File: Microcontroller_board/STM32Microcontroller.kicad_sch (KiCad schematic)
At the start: 0 parts

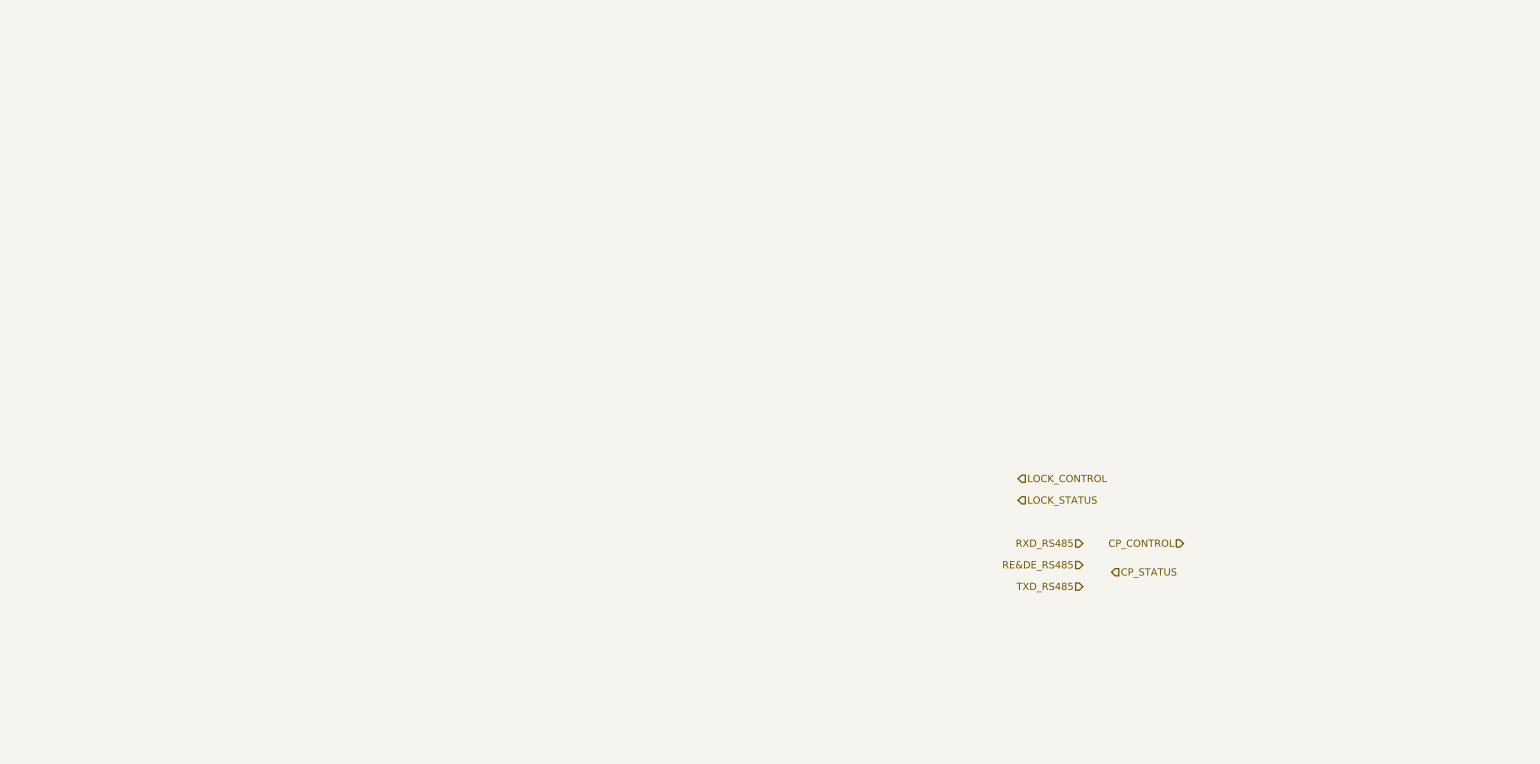
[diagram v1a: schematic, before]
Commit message: CP circuit added as in the PRIMO charger
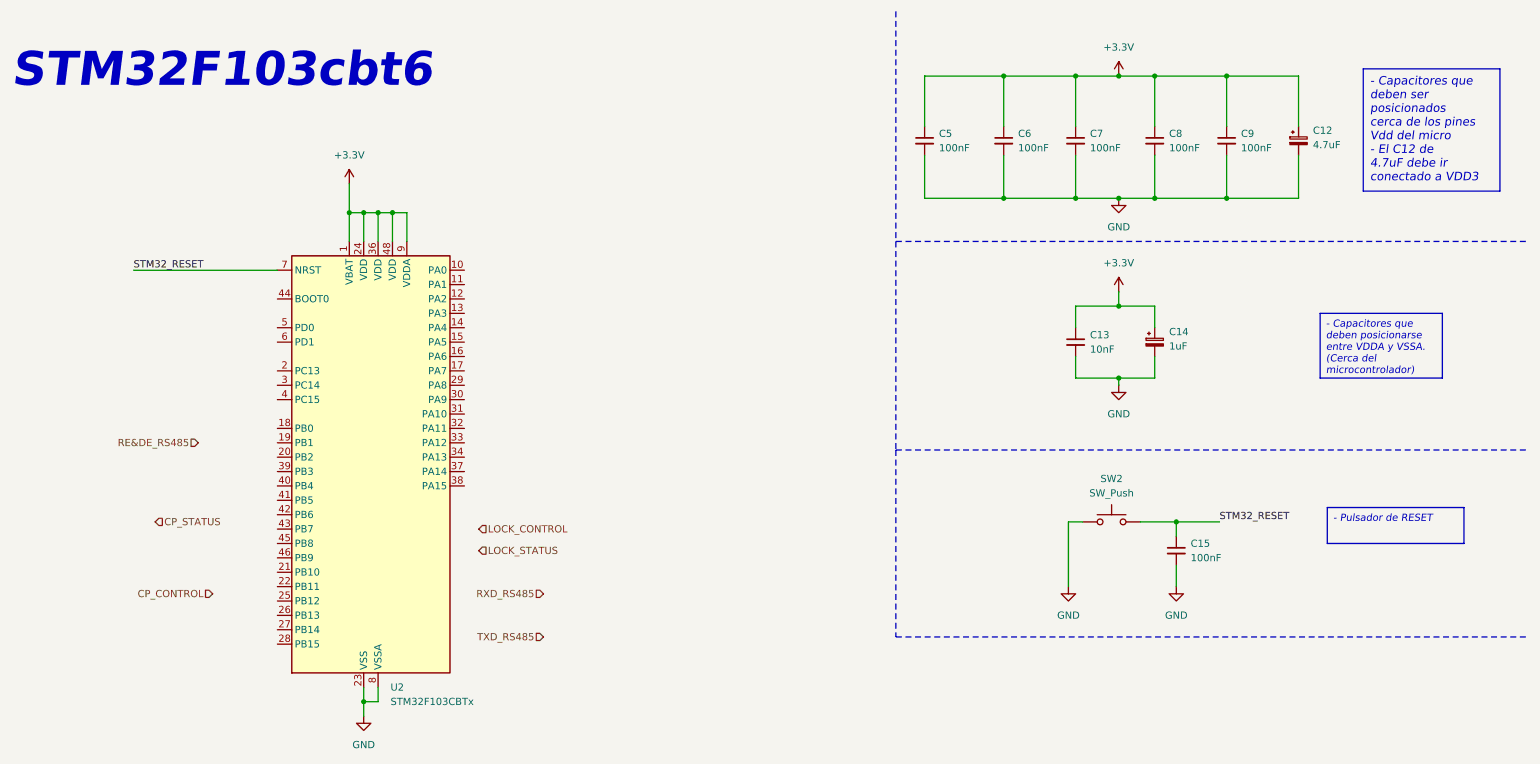
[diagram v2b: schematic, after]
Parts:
- added C12: 4.7uF, symbol Device:C_Polarized_Small
- added C13: 10nF, symbol Device:C_Small
- added C14: 1uF, symbol Device:C_Polarized_Small
- added C15, C5, C6, C7, C8, C9: 100nF, symbol Device:C_Small
- added SW2: SW_Push, symbol Switch:SW_Push
- added U2: STM32F103CBTx, Package_QFP:LQFP-48_7x7mm_P0.5mm, symbol MCU_ST_STM32F1:STM32F103CBTx
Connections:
- new net +3.3V: C12.1, C13.1, C14.1, C5.1, C6.1, C7.1, C8.1, C9.1, U2.1 (VBAT), U2.24 (VDD), U2.36 (VDD), U2.48 (VDD), U2.9 (VDDA)
- new net GND: C12.2, C13.2, C14.2, C15.2, C5.2, C6.2, C7.2, C8.2, C9.2, SW2.1, U2.23 (VSS), U2.35 (VSS), U2.47 (VSS), U2.8 (VSSA)
- new net STM32_RESET: C15.1, SW2.2, U2.7 (NRST)
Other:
- note added: "STM32F103cbt6"

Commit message: Added led interface
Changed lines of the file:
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@@
   )
   (text_box "- Pulsador de RESET"
-    (at 248.92 99.06 0) (size 24.13 6.35)
+    (at 256.54 99.06 0) (size 24.13 6.35)
     (stroke (width 0) (type default))
     (fill (type color) (color 255 227 142 1))
@@
   )
   (text_box "- Capacitores que deben ser posicionados cerca de los pines Vdd del micro\n- El C12 de 4.7uF debe ir conectado a VDD3\n\n"
-    (at 255.27 21.59 0) (size 24.13 21.59)
+    (at 255.27 21.59 0) (size 25.4 22.86)
     (stroke (width 0) (type default))
     (fill (type color) (color 255 227 142 1))
@@
   )
   (text_box "- Capacitores que deben posicionarse entre VDDA y VSSA.\n(Cerca del microcontrolador)"
-    (at 247.65 64.77 0) (size 21.59 11.43)
+    (at 256.54 64.77 0) (size 24.13 12.7)
     (stroke (width 0) (type default))
     (fill (type color) (color 255 227 142 1))
@@
     (effects (font (size 1.27 1.27)) (justify right))
   )
+  (hierarchical_label "LED_CONTROL" (shape input) (at 99.06 125.73 0) (fields_autoplaced)
+    (effects (font (size 1.27 1.27)) (justify left))
+  )
   (hierarchical_label "RE&DE_RS485" (shape input) (at 49.53 87.63 180) (fields_autoplaced)

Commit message: Added connector for st link programmer
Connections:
- net SWDIO: now reaches U2.34 (PA13)
- net SWCLK: now reaches U2.37 (PA14)
- net STM32_RESET renamed NRST
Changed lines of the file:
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@@
-    (stroke (width 0) (type default))
-  )
-  (wire (pts (xy 38.1 57.15) (xy 63.5 57.15))
     (stroke (width 0) (type default))
   )
@@
     (stroke (width 0) (type default))
   )
+  (wire (pts (xy 96.52 90.17) (xy 104.14 90.17))
+    (stroke (width 0) (type default))
+  )
+  (wire (pts (xy 96.52 92.71) (xy 104.14 92.71))
+    (stroke (width 0) (type default))
+  )
   (wire (pts (xy 231.14 22.86) (xy 218.44 22.86))
     (stroke (width 0) (type default))
@@
   )
   (wire (pts (xy 177.8 44.45) (xy 191.77 44.45))
+    (stroke (width 0) (type default))
+  )
+  (wire (pts (xy 49.53 57.15) (xy 63.5 57.15))
     (stroke (width 0) (type default))
   )
@@
     (effects (font (size 6 6) (thickness 1.2) bold italic) (justify left bottom))
   )
-  (label "STM32_RESET" (at 229.87 101.6 0) (fields_autoplaced)
-    (effects (font (size 1.27 1.27)) (justify left bottom))
-  )
-  (label "STM32_RESET" (at 38.1 57.15 0) (fields_autoplaced)
-    (effects (font (size 1.27 1.27)) (justify left bottom))
-  )
   (hierarchical_label "CP_CONTROL" (shape input) (at 52.07 114.3 180) (fields_autoplaced)
     (effects (font (size 1.27 1.27)) (justify right))
@@
     (effects (font (size 1.27 1.27)) (justify left))
   )
+  (hierarchical_label "NRST" (shape input) (at 229.87 101.6 0) (fields_autoplaced)
+    (effects (font (size 1.27 1.27)) (justify left))
+  )
+  (hierarchical_label "SWCLK" (shape input) (at 104.14 92.71 0) (fields_autoplaced)
+    (effects (font (size 1.27 1.27)) (justify left))
+  )
   (hierarchical_label "RE&DE_RS485" (shape input) (at 49.53 87.63 180) (fields_autoplaced)
     (effects (font (size 1.27 1.27)) (justify right))
   )
+  (hierarchical_label "NRST" (shape input) (at 49.53 57.15 180) (fields_autoplaced)
+    (effects (font (size 1.27 1.27)) (justify right))
+  )
   (hierarchical_label "CP_STATUS" (shape input) (at 41.91 101.6 0) (fields_autoplaced)
     (effects (font (size 1.27 1.27)) (justify left))
   )
+  (hierarchical_label "SWDIO" (shape input) (at 104.14 90.17 0) (fields_autoplaced)
+    (effects (font (size 1.27 1.27)) (justify left))
+  )
